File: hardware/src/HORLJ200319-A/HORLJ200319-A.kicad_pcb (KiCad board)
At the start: 2 copper layers, 30 x 30 mm, 63 parts, among them U1 ATmega328P-MMH

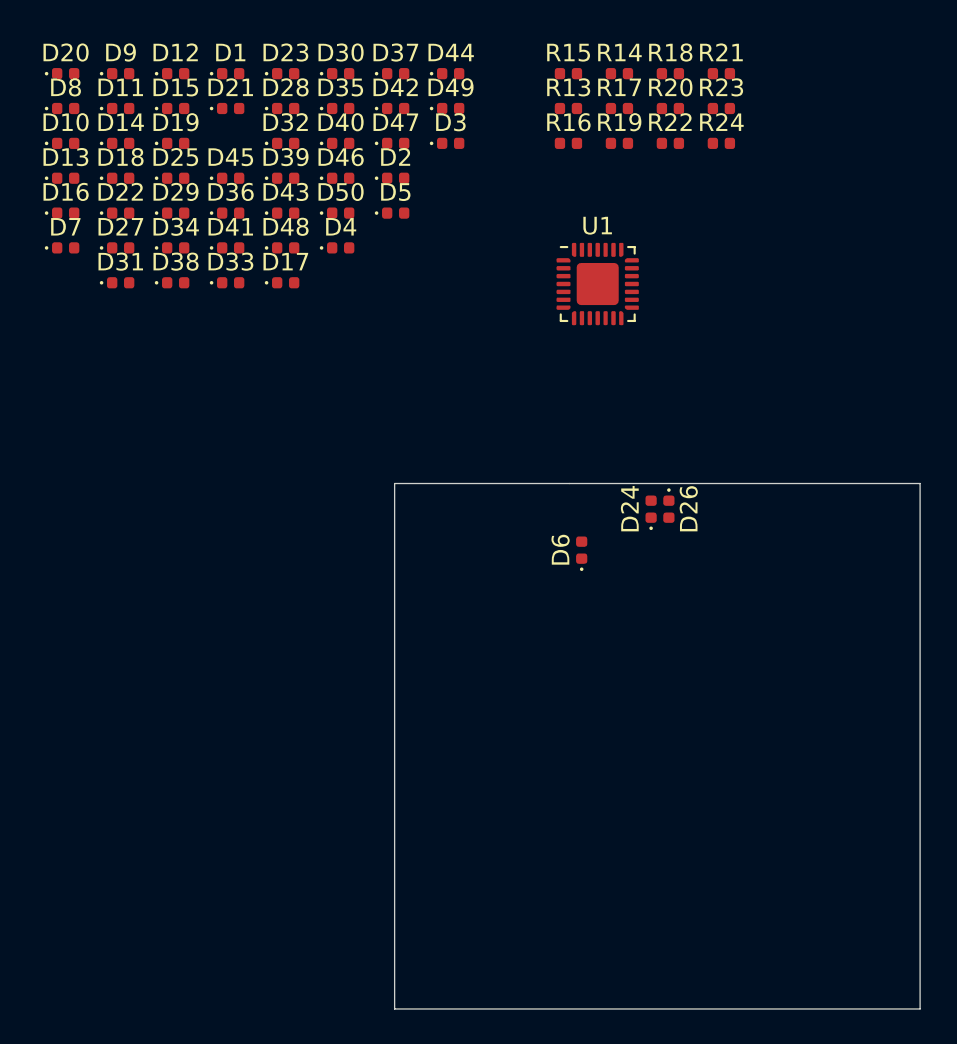
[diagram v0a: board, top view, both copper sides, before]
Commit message: Insere MockUps digitais e inicia o projeto da PCB.
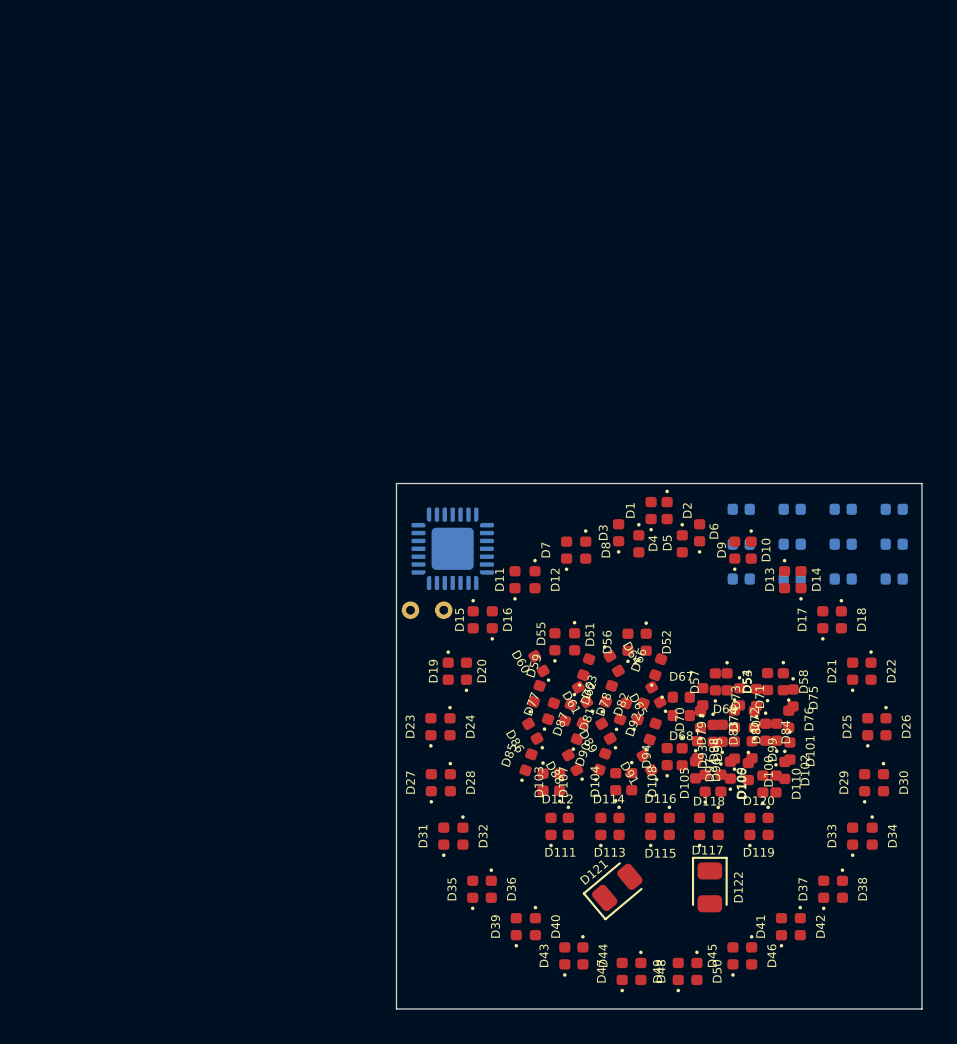
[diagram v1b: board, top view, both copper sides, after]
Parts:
- removed R13, R14, R15, R16, R17, R18, R19, R20, R21, R22, R23, R24: 100R, Resistor_SMD:R_0402_1005Metric
- added D100: GREEN, LED_SMD:LED_0402_1005Metric, F.Cu at (70.2, 141.4)
- added D101: RED, LED_SMD:LED_0402_1005Metric, F.Cu at (72.6, 140.3)
- added D102: GREEN, LED_SMD:LED_0402_1005Metric, F.Cu at (72.3, 141.4)
- added D103: GREEN, LED_SMD:LED_0402_1005Metric, F.Cu at (59.4, 142.0)
- added D104: GREEN, LED_SMD:LED_0402_1005Metric, F.Cu at (62.6, 142.0)
- added D105: GREEN, LED_SMD:LED_0402_1005Metric, F.Cu at (67.7, 142.1)
- added D106: GREEN, LED_SMD:LED_0402_1005Metric, F.Cu at (71.0, 142.2)
- added D107: RED, LED_SMD:LED_0402_1005Metric, F.Cu at (58.5, 142.0)
- added D108: RED, LED_SMD:LED_0402_1005Metric, F.Cu at (63.5, 142.0)
- added D109: RED, LED_SMD:LED_0402_1005Metric, F.Cu at (68.6, 142.1)
- added D110: RED, LED_SMD:LED_0402_1005Metric, F.Cu at (71.8, 142.2)
- added D111: RED, LED_SMD:LED_0402_1005Metric, F.Cu at (58.9, 144.6)
- added D112: GREEN, LED_SMD:LED_0402_1005Metric, F.Cu at (59.9, 144.6)
- added D113: RED, LED_SMD:LED_0402_1005Metric, F.Cu at (61.8, 144.6)
- added D114: GREEN, LED_SMD:LED_0402_1005Metric, F.Cu at (62.8, 144.6)
- added D115: RED, LED_SMD:LED_0402_1005Metric, F.Cu at (64.6, 144.6)
- added D116: GREEN, LED_SMD:LED_0402_1005Metric, F.Cu at (65.7, 144.6)
- added D117: RED, LED_SMD:LED_0402_1005Metric, F.Cu at (67.4, 144.6)
- added D118: GREEN, LED_SMD:LED_0402_1005Metric, F.Cu at (68.5, 144.6)
- added D119: RED, LED_SMD:LED_0402_1005Metric, F.Cu at (70.3, 144.6)
- added D120: GREEN, LED_SMD:LED_0402_1005Metric, F.Cu at (71.3, 144.6)
- added D121: RED, LED_SMD:LED_0805_2012Metric, F.Cu at (62.7, 148.1)
- added D122: GREEN, LED_SMD:LED_0805_2012Metric, F.Cu at (68.0, 148.1)
- added D51: GREEN, LED_SMD:LED_0402_1005Metric, F.Cu at (60.3, 134.0)
- added D52: GREEN, LED_SMD:LED_0402_1005Metric, F.Cu at (64.4, 134.1)
- added D53: GREEN, LED_SMD:LED_0402_1005Metric, F.Cu at (69.0, 136.3)
- added D54: GREEN, LED_SMD:LED_0402_1005Metric, F.Cu at (71.3, 136.3)
- added D55: RED, LED_SMD:LED_0402_1005Metric, F.Cu at (59.1, 134.0)
- added D56: RED, LED_SMD:LED_0402_1005Metric, F.Cu at (63.3, 134.1)
- added D57: RED, LED_SMD:LED_0402_1005Metric, F.Cu at (68.3, 136.3)
- added D58: RED, LED_SMD:LED_0402_1005Metric, F.Cu at (72.2, 136.3)
- added D59: RED, LED_SMD:LED_0402_1005Metric, F.Cu at (58.1, 137.0)
- added D60: GREEN, LED_SMD:LED_0402_1005Metric, F.Cu at (58.2, 135.3)
- added D61: RED, LED_SMD:LED_0402_1005Metric, F.Cu at (60.7, 137.1)
- added D62: GREEN, LED_SMD:LED_0402_1005Metric, F.Cu at (60.9, 135.5)
- added D63: RED, LED_SMD:LED_0402_1005Metric, F.Cu at (62.2, 137.0)
- added D64: GREEN, LED_SMD:LED_0402_1005Metric, F.Cu at (62.5, 135.3)
- added D65: RED, LED_SMD:LED_0402_1005Metric, F.Cu at (64.9, 137.1)
- added D66: GREEN, LED_SMD:LED_0402_1005Metric, F.Cu at (65.0, 135.5)
- added D67: RED, LED_SMD:LED_0402_1005Metric, F.Cu at (66.4, 137.2)
- added D68: GREEN, LED_SMD:LED_0402_1005Metric, F.Cu at (66.4, 138.2)
- added D69: RED, LED_SMD:LED_0402_1005Metric, F.Cu at (67.6, 137.2)
- added D70: GREEN, LED_SMD:LED_0402_1005Metric, F.Cu at (67.5, 138.5)
- added D71: RED, LED_SMD:LED_0402_1005Metric, F.Cu at (69.7, 137.2)
- added D72: GREEN, LED_SMD:LED_0402_1005Metric, F.Cu at (69.4, 138.4)
- added D73: RED, LED_SMD:LED_0402_1005Metric, F.Cu at (70.7, 137.2)
- added D74: GREEN, LED_SMD:LED_0402_1005Metric, F.Cu at (70.5, 138.5)
- added D75: RED, LED_SMD:LED_0402_1005Metric, F.Cu at (72.8, 137.2)
- added D76: GREEN, LED_SMD:LED_0402_1005Metric, F.Cu at (72.5, 138.5)
- added D77: GREEN, LED_SMD:LED_0402_1005Metric, F.Cu at (58.9, 138.0)
- added D78: GREEN, LED_SMD:LED_0402_1005Metric, F.Cu at (63.0, 138.0)
- added D79: GREEN, LED_SMD:LED_0402_1005Metric, F.Cu at (68.7, 139.3)
- added D80: GREEN, LED_SMD:LED_0402_1005Metric, F.Cu at (71.8, 139.2)
- added D81: RED, LED_SMD:LED_0402_1005Metric, F.Cu at (59.9, 138.1)
- added D82: RED, LED_SMD:LED_0402_1005Metric, F.Cu at (64.0, 138.0)
- added D83: RED, LED_SMD:LED_0402_1005Metric, F.Cu at (68.2, 139.3)
- added D84: RED, LED_SMD:LED_0402_1005Metric, F.Cu at (71.2, 139.2)
- added D85: RED, LED_SMD:LED_0402_1005Metric, F.Cu at (57.6, 140.9)
- added D86: GREEN, LED_SMD:LED_0402_1005Metric, F.Cu at (57.9, 139.1)
- added D87: RED, LED_SMD:LED_0402_1005Metric, F.Cu at (60.6, 139.1)
- added D88: GREEN, LED_SMD:LED_0402_1005Metric, F.Cu at (60.2, 140.9)
- added D89: RED, LED_SMD:LED_0402_1005Metric, F.Cu at (62.1, 139.1)
- added D90: GREEN, LED_SMD:LED_0402_1005Metric, F.Cu at (61.9, 140.9)
- added D91: RED, LED_SMD:LED_0402_1005Metric, F.Cu at (64.4, 141.0)
- added D92: GREEN, LED_SMD:LED_0402_1005Metric, F.Cu at (64.7, 139.2)
- added D93: RED, LED_SMD:LED_0402_1005Metric, F.Cu at (66.4, 140.6)
- added D94: GREEN, LED_SMD:LED_0402_1005Metric, F.Cu at (65.6, 140.6)
- added D95: RED, LED_SMD:LED_0402_1005Metric, F.Cu at (67.3, 140.2)
- added D96: GREEN, LED_SMD:LED_0402_1005Metric, F.Cu at (67.2, 141.3)
- added D97: RED, LED_SMD:LED_0402_1005Metric, F.Cu at (69.2, 141.4)
- added D98: GREEN, LED_SMD:LED_0402_1005Metric, F.Cu at (69.4, 140.2)
- added D99: RED, LED_SMD:LED_0402_1005Metric, F.Cu at (70.4, 140.2)
- added R1: 100R, Resistor_SMD:R_0402_1005Metric, B.Cu at (69.8, 128.5)
- added R10: 100R, Resistor_SMD:R_0402_1005Metric, B.Cu at (75.6, 126.5)
- added R11: 100R, Resistor_SMD:R_0402_1005Metric, B.Cu at (78.5, 128.5)
- added R12: 100R, Resistor_SMD:R_0402_1005Metric, B.Cu at (78.5, 126.5)
- added R2: 100R, Resistor_SMD:R_0402_1005Metric, B.Cu at (72.7, 130.5)
- added R3: 100R, Resistor_SMD:R_0402_1005Metric, B.Cu at (69.8, 126.5)
- added R4: 100R, Resistor_SMD:R_0402_1005Metric, B.Cu at (69.8, 130.5)
- added R5: 100R, Resistor_SMD:R_0402_1005Metric, B.Cu at (72.7, 128.5)
- added R6: 100R, Resistor_SMD:R_0402_1005Metric, B.Cu at (75.6, 130.5)
- added R7: 100R, Resistor_SMD:R_0402_1005Metric, B.Cu at (72.7, 126.5)
- added R8: 100R, Resistor_SMD:R_0402_1005Metric, B.Cu at (75.6, 128.5)
- added R9: 100R, Resistor_SMD:R_0402_1005Metric, B.Cu at (78.5, 130.5)
- added Y1: 32.768kHz, Crystal:Crystal_C26-LF_D2.1mm_L6.5mm_Horizontal, B.Cu at (52.8, 132.2)
- D10, D14, D18, D2, D22, D24, D28, D32, D36, D4, D40, D42, D46: value RED -> GREEN
- D11, D15, D19, D23, D25, D29, D33, D37, D41, D47, D49, D5, D7: value GREEN -> RED
- U1: moved to B.Cu
- moved D45 52.9 mm to (69.3, 152.0), turned to 90 degrees
- moved D37 52.6 mm to (74.5, 148.2), turned to 90 degrees
- moved D42 52.1 mm to (73.2, 150.3), turned to 270 degrees
- moved D34 52.0 mm to (77.3, 145.1), turned to 270 degrees
- moved D38 51.5 mm to (75.6, 148.2), turned to 270 degrees
- moved D29 51.0 mm to (76.8, 142.1), turned to 90 degrees
- moved D30 51.0 mm to (77.9, 142.1), turned to 270 degrees
- moved D49 51.0 mm to (66.2, 152.9), turned to 90 degrees
- moved D44 50.9 mm to (60.7, 152.0), turned to 270 degrees
- moved D25 50.4 mm to (77.0, 138.9), turned to 90 degrees
- moved D46 50.2 mm to (70.4, 152.0), turned to 270 degrees
- moved D22 50.2 mm to (77.2, 135.7), turned to 270 degrees
- moved D41 49.9 mm to (72.1, 150.3), turned to 90 degrees
- moved D47 49.0 mm to (63.0, 152.9), turned to 90 degrees
- moved D18 48.3 mm to (75.5, 132.8), turned to 270 degrees
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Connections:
- D1 pad 1: /Display Structure/Display Chronograph/DBUS_02 -> DBUS_01
- D1 pad 2: /Display Structure/Display Chronograph/DBUS_11 -> DBUS_02
- D10 pad 1: /Display Structure/Display Chronograph/DBUS_02 -> DBUS_04
- D10 pad 2: /Display Structure/Display Chronograph/DBUS_08 -> DBUS_01
- D11 pad 1: /Display Structure/Display Chronograph/DBUS_04 -> DBUS_03
- D11 pad 2: /Display Structure/Display Chronograph/DBUS_03 -> DBUS_05
- D12 pad 1: /Display Structure/Display Chronograph/DBUS_08 -> DBUS_05
- D12 pad 2: /Display Structure/Display Chronograph/DBUS_02 -> DBUS_03
- D13 pad 1: /Display Structure/Display Chronograph/DBUS_03 -> DBUS_01
- D13 pad 2: /Display Structure/Display Chronograph/DBUS_05 -> DBUS_05
- D14 pad 1: /Display Structure/Display Chronograph/DBUS_02 -> DBUS_05
- D14 pad 2: /Display Structure/Display Chronograph/DBUS_07 -> DBUS_01
- D15 pad 1: /Display Structure/Display Chronograph/DBUS_05 -> DBUS_03
- D15 pad 2: /Display Structure/Display Chronograph/DBUS_03 -> DBUS_04
- D16 pad 1: /Display Structure/Display Chronograph/DBUS_07 -> DBUS_04
- D16 pad 2: /Display Structure/Display Chronograph/DBUS_02 -> DBUS_03
- D17 pad 1: /Display Structure/Display Chronograph/DBUS_03 -> DBUS_01
- D17 pad 2: /Display Structure/Display Chronograph/DBUS_06 -> DBUS_06
- D18 pad 1: /Display Structure/Display Chronograph/DBUS_02 -> DBUS_06
- D18 pad 2: /Display Structure/Display Chronograph/DBUS_06 -> DBUS_01
- D19 pad 1: /Display Structure/Display Chronograph/DBUS_06 -> DBUS_02
- D19 pad 2: /Display Structure/Display Chronograph/DBUS_03 -> DBUS_12
- D2 pad 1: /Display Structure/Display Chronograph/DBUS_02 -> DBUS_02
- D2 pad 2: /Display Structure/Display Chronograph/DBUS_10 -> DBUS_01
- D20 pad 1: /Display Structure/Display Chronograph/DBUS_06 -> DBUS_12
- D20 pad 2: /Display Structure/Display Chronograph/DBUS_02 -> DBUS_02
- D21 pad 1: /Display Structure/Display Chronograph/DBUS_03 -> DBUS_01
- D21 pad 2: /Display Structure/Display Chronograph/DBUS_07 -> DBUS_07
- D22 pad 1: /Display Structure/Display Chronograph/DBUS_02 -> DBUS_07
- D22 pad 2: /Display Structure/Display Chronograph/DBUS_05 -> DBUS_01
- D23 pad 1: /Display Structure/Display Chronograph/DBUS_07 -> DBUS_02
- D23 pad 2: /Display Structure/Display Chronograph/DBUS_03 -> DBUS_11
- D24 pad 1: /Display Structure/Display Chronograph/DBUS_01 -> DBUS_11
- D24 pad 2: /Display Structure/Display Chronograph/DBUS_02 -> DBUS_02
- D25 pad 1: /Display Structure/Display Chronograph/DBUS_05 -> DBUS_01
- D25 pad 2: /Display Structure/Display Chronograph/DBUS_02 -> DBUS_08
- D26 pad 1: /Display Structure/Display Chronograph/DBUS_02 -> DBUS_08
- D26 pad 2: /Display Structure/Display Chronograph/DBUS_01 -> DBUS_01
- D27 pad 1: /Display Structure/Display Chronograph/DBUS_01 -> DBUS_02
- D27 pad 2: /Display Structure/Display Chronograph/DBUS_03 -> DBUS_10
- D28 pad 1: /Display Structure/Display Chronograph/DBUS_02 -> DBUS_10
- D28 pad 2: /Display Structure/Display Chronograph/DBUS_04 -> DBUS_02
- D29 pad 1: /Display Structure/Display Chronograph/DBUS_03 -> DBUS_01
- D29 pad 2: /Display Structure/Display Chronograph/DBUS_01 -> DBUS_09
- D3 pad 1: /Display Structure/Display Chronograph/DBUS_02 -> DBUS_03
- D3 pad 2: /Display Structure/Display Chronograph/DBUS_12 -> DBUS_07
- D30 pad 1: /Display Structure/Display Chronograph/DBUS_04 -> DBUS_09
- D30 pad 2: /Display Structure/Display Chronograph/DBUS_02 -> DBUS_01
- D31 pad 1: /Display Structure/Display Chronograph/DBUS_02 -> DBUS_02
- D31 pad 2: /Display Structure/Display Chronograph/DBUS_03 -> DBUS_09
- D32 pad 1: /Display Structure/Display Chronograph/DBUS_01 -> DBUS_09
- D32 pad 2: /Display Structure/Display Chronograph/DBUS_04 -> DBUS_02
- D33 pad 1: /Display Structure/Display Chronograph/DBUS_03 -> DBUS_01
- D33 pad 2: /Display Structure/Display Chronograph/DBUS_02 -> DBUS_10
- D34 pad 1: /Display Structure/Display Chronograph/DBUS_04 -> DBUS_10
- D34 pad 2: /Display Structure/Display Chronograph/DBUS_01 -> DBUS_01
- D35 pad 1: /Display Structure/Display Chronograph/DBUS_01 -> DBUS_02
- D35 pad 2: /Display Structure/Display Chronograph/DBUS_05 -> DBUS_08
- D36 pad 1: /Display Structure/Display Chronograph/DBUS_01 -> DBUS_08
- D36 pad 2: /Display Structure/Display Chronograph/DBUS_12 -> DBUS_02
- D37 pad 1: /Display Structure/Display Chronograph/DBUS_05 -> DBUS_01
- D37 pad 2: /Display Structure/Display Chronograph/DBUS_01 -> DBUS_11
- D38 pad 1: /Display Structure/Display Chronograph/DBUS_12 -> DBUS_11
- D38 pad 2: /Display Structure/Display Chronograph/DBUS_01 -> DBUS_01
- D39 pad 1: /Display Structure/Display Chronograph/DBUS_01 -> DBUS_02
- D39 pad 2: /Display Structure/Display Chronograph/DBUS_06 -> DBUS_07
- D4 pad 1: /Display Structure/Display Chronograph/DBUS_02 -> DBUS_07
- D4 pad 2: /Display Structure/Display Chronograph/DBUS_09 -> DBUS_03
- D40 pad 1: /Display Structure/Display Chronograph/DBUS_01 -> DBUS_07
- D40 pad 2: /Display Structure/Display Chronograph/DBUS_11 -> DBUS_02
- D41 pad 1: /Display Structure/Display Chronograph/DBUS_06 -> DBUS_01
- D41 pad 2: /Display Structure/Display Chronograph/DBUS_01 -> DBUS_12
- D42 pad 1: /Display Structure/Display Chronograph/DBUS_01 -> DBUS_12
- D42 pad 2: /Display Structure/Display Chronograph/DBUS_07 -> DBUS_01
- D43 pad 1: /Display Structure/Display Chronograph/DBUS_01 -> DBUS_02
- D43 pad 2: /Display Structure/Display Chronograph/DBUS_10 -> DBUS_06
- D44 pad 1: /Display Structure/Display Chronograph/DBUS_11 -> DBUS_06
- D44 pad 2: /Display Structure/Display Chronograph/DBUS_01 -> DBUS_02
- D45 pad 1: /Display Structure/Display Chronograph/DBUS_01 -> DBUS_02
- D45 pad 2: /Display Structure/Display Chronograph/DBUS_08 -> DBUS_03
- D46 pad 1: /Display Structure/Display Chronograph/DBUS_01 -> DBUS_03
- D46 pad 2: /Display Structure/Display Chronograph/DBUS_09 -> DBUS_02
- D47 pad 1: /Display Structure/Display Chronograph/DBUS_07 -> DBUS_02
- D47 pad 2: /Display Structure/Display Chronograph/DBUS_01 -> DBUS_05
- D48 pad 1: /Display Structure/Display Chronograph/DBUS_10 -> DBUS_05
- D48 pad 2: /Display Structure/Display Chronograph/DBUS_01 -> DBUS_02
- D49 pad 1: /Display Structure/Display Chronograph/DBUS_08 -> DBUS_02
- D49 pad 2: /Display Structure/Display Chronograph/DBUS_01 -> DBUS_04
- D5 pad 1: /Display Structure/Display Chronograph/DBUS_11 -> DBUS_01
- D5 pad 2: /Display Structure/Display Chronograph/DBUS_02 -> DBUS_03
- D50 pad 1: /Display Structure/Display Chronograph/DBUS_09 -> DBUS_04
- D50 pad 2: /Display Structure/Display Chronograph/DBUS_01 -> DBUS_02
- D6 pad 1: /Display Structure/Display Chronograph/DBUS_10 -> DBUS_03
- D6 pad 2: /Display Structure/Display Chronograph/DBUS_02 -> DBUS_01
- D7 pad 1: /Display Structure/Display Chronograph/DBUS_12 -> DBUS_03
- D7 pad 2: /Display Structure/Display Chronograph/DBUS_02 -> DBUS_06
- D8 pad 1: /Display Structure/Display Chronograph/DBUS_09 -> DBUS_06
- D8 pad 2: /Display Structure/Display Chronograph/DBUS_02 -> DBUS_03
- D9 pad 1: /Display Structure/Display Chronograph/DBUS_03 -> DBUS_01
- D9 pad 2: /Display Structure/Display Chronograph/DBUS_04 -> DBUS_04
- U1 pad 1: Net-(U1-Pad1) -> /PD3
- U1 pad 10: Net-(U1-Pad10) -> /PB0
- U1 pad 11: Net-(U1-Pad11) -> /PB1
- U1 pad 12: Net-(U1-Pad12) -> /PB2
- U1 pad 13: /Microcontroller Unity/SPI_MOSI -> /PB3
- U1 pad 14: /Microcontroller Unity/SPI_MISO -> /PB4
- U1 pad 15: /Microcontroller Unity/SPI_SCK -> /PB5
- U1 pad 2: Net-(U1-Pad2) -> /PD4
- U1 pad 28: Net-(U1-Pad28) -> /PD2
- U1 pad 7: SW_SIGNAL -> /PD5
- U1 pad 8: Net-(U1-Pad8) -> /PD6
- U1 pad 9: Net-(U1-Pad9) -> /PD7
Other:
- outline, holes or cut-outs redrawn
- net class Default: clearance 0.2 -> 0.254; trace_width 0.25 -> 0.3
- rule trace_clearance: 0.2 -> 0.254
